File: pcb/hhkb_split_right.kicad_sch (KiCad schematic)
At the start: 82 parts, among them SW1 keyswitch, SW10 keyswitch, SW11 keyswitch, SW12 keyswitch, SW13 keyswitch, SW14 keyswitch, SW15 keyswitch, SW16 keyswitch, SW17 keyswitch, SW18 keyswitch, SW19 keyswitch, SW2 keyswitch, SW20 keyswitch, SW21 keyswitch, SW22 keyswitch, SW23 keyswitch, SW24 keyswitch, SW25 keyswitch, SW26 keyswitch, SW27 keyswitch, SW28 keyswitch, SW29 keyswitch, SW3 keyswitch, SW30 keyswitch, SW31 keyswitch, SW32 keyswitch, SW33 keyswitch, SW34 keyswitch, SW4 keyswitch, SW5 keyswitch, SW6 keyswitch, SW7 keyswitch, SW8 keyswitch, SW9 keyswitch, U1 74LVC595, U2 74LVC595

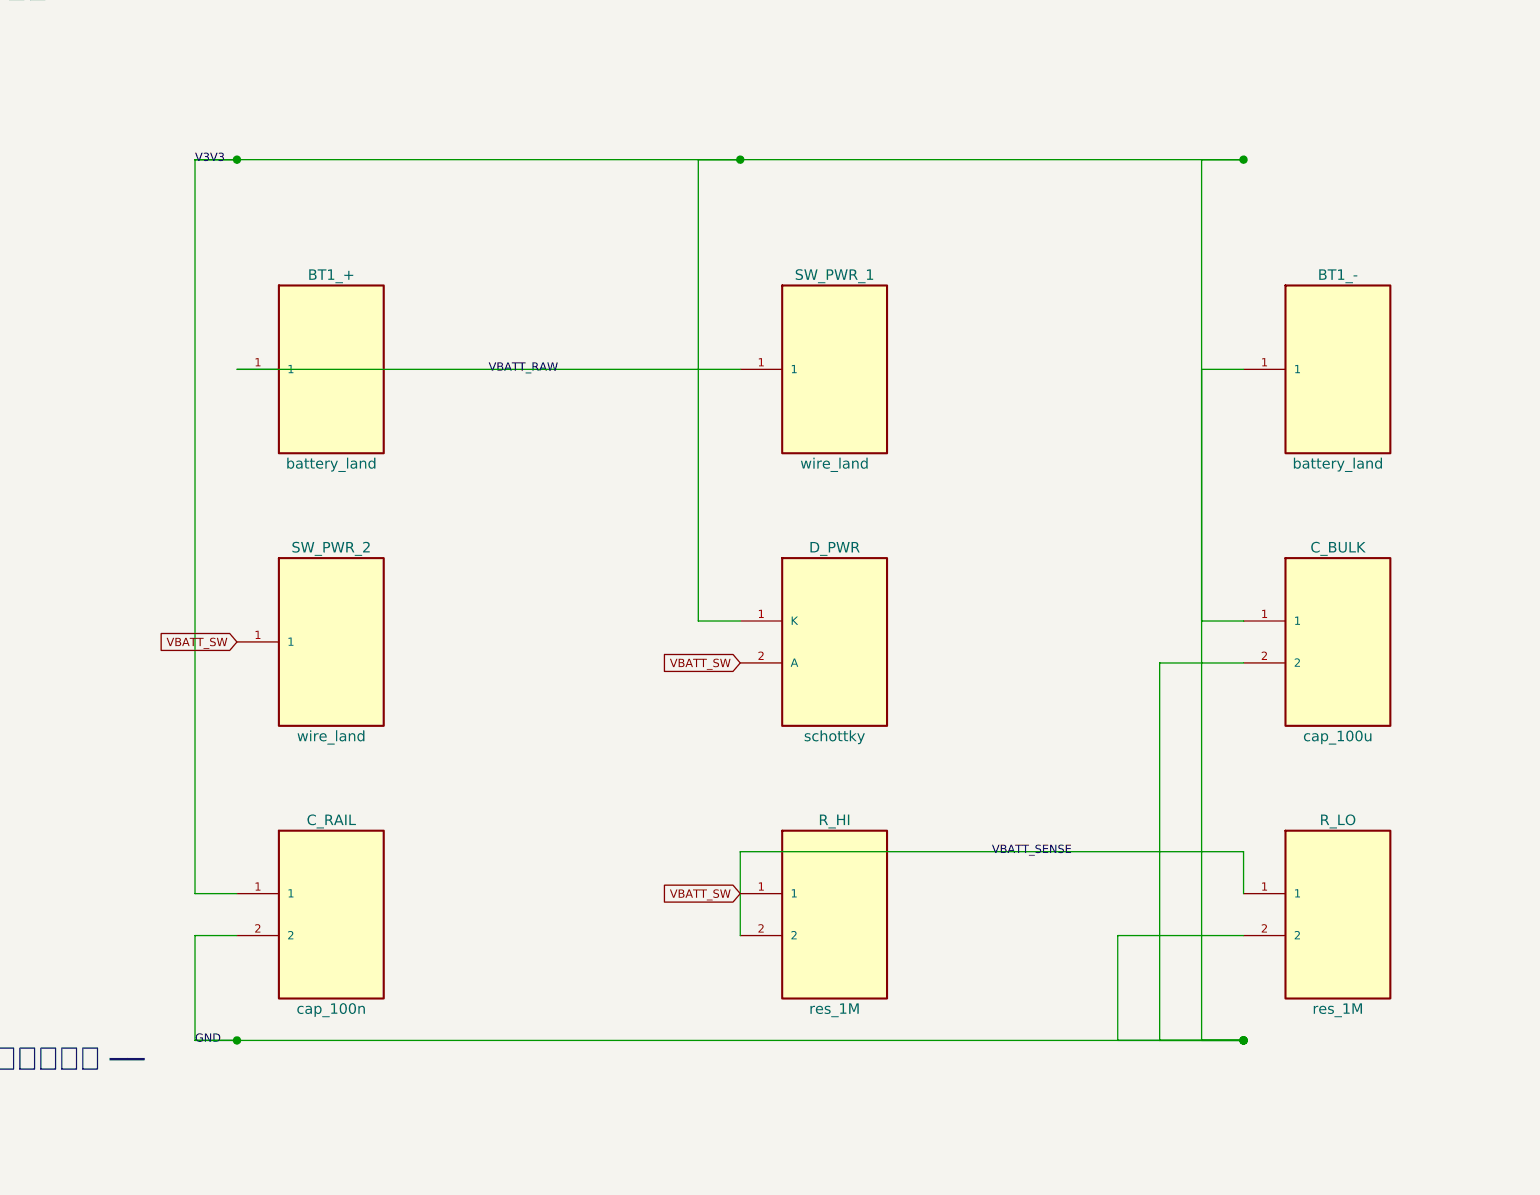
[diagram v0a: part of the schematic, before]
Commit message: C_RAIL を消した。置き場所の根拠が持たず C_U1 の重複だった
open-gaps #39 は「U1 の隣か J_DB の隣か」で止まっていたが、二択の
立て方が違った。FFC の反対側の C_DB を数えると、U_MCU から 3.95mm の
XIAO 用パスコンで、FFC 入口ではない。つまりケーブル入口のパスコンは
もともと両端どちらにも無く、片端だけ手当てする案は理屈が対称にならない。

C_RAIL は実測で J_DB から 70mm、C_U1 の 5.1mm 隣にあった（J_DB を
帯 1 へ移したときに取り残された）。名前どおりの役目は果たしていない。

消した理由は「不要と証明できたから」ではなく、必要と言える根拠が
1 つも無く、各 IC が既に自分の直近パスコンを持つから（595 は
C_U1/C_U2、XIAO は C_DB、レールは C_BULK）。

DRC 違反は左右子とも 0 のまま。右だけ未配線が 0 → 1 に増えた。中身は
信号線ではなく、(152.65, 68.37) の GND スティッチングビアがベタから
浮いたもの（C_RAIL の跡地）。自動配線 2 回で同じなので構造的。
配線に大きな変更が控えているため、それと併せて確認する（open-gaps #40）。

⚠️ pytest tools は最後まで通していない。次の配線変更とまとめて回す。

Co-Authored-By: Claude Opus 5 (1M context) <noreply@anthropic.com>
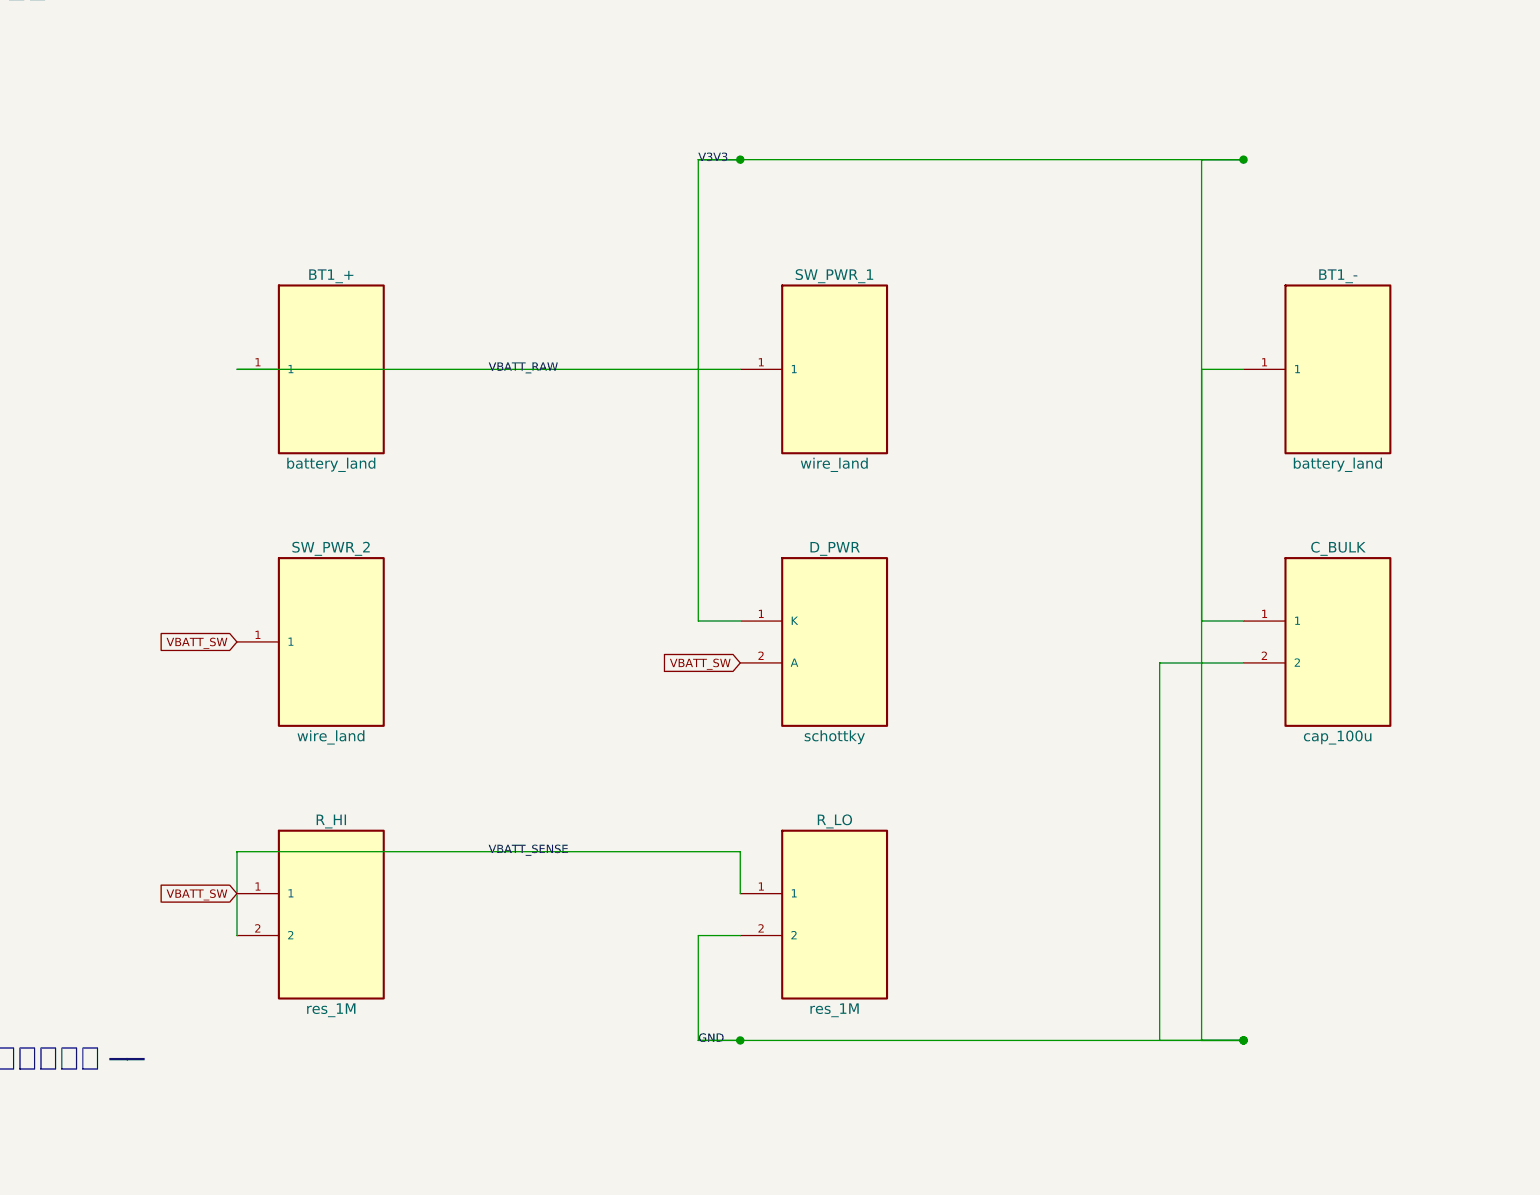
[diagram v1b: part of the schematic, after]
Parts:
- removed C_RAIL: cap_100n, symbol hhkb_split_right:cap_100n
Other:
- moved on the sheet: R_HI, R_LO
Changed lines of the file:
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@@
 		"VBATT_SW"
 		(shape input)
-		(at 124.46 132.08 180)
+		(at 63.50 132.08 180)
 		(effects (font (size 1.0 1.0)))
 	)
@@
 	)
 	(wire
-		(pts (xy 58.42 43.18) (xy 185.42 43.18))
+		(pts (xy 119.38 43.18) (xy 185.42 43.18))
 		(stroke (width 0.508) (type default))
 	)
 	(label
 		"V3V3"
-		(at 58.42 43.18 0)
-		(effects (font (size 1.0 1.0)))
-	)
-	(wire
-		(pts (xy 58.42 149.86) (xy 185.42 149.86))
+		(at 119.38 43.18 0)
+		(effects (font (size 1.0 1.0)))
+	)
+	(wire
+		(pts (xy 119.38 149.86) (xy 185.42 149.86))
 		(stroke (width 0.508) (type default))
 	)
 	(label
 		"GND"
-		(at 58.42 149.86 0)
+		(at 119.38 149.86 0)
 		(effects (font (size 1.0 1.0)))
 	)
@@
 	)
 	(wire
-		(pts (xy 124.46 137.16) (xy 124.46 127.00))
-		(stroke (width 0) (type default))
-	)
-	(wire
-		(pts (xy 124.46 127.00) (xy 185.42 127.00))
-		(stroke (width 0) (type default))
-	)
-	(wire
-		(pts (xy 185.42 127.00) (xy 185.42 132.08))
+		(pts (xy 63.50 137.16) (xy 63.50 127.00))
+		(stroke (width 0) (type default))
+	)
+	(wire
+		(pts (xy 63.50 127.00) (xy 124.46 127.00))
+		(stroke (width 0) (type default))
+	)
+	(wire
+		(pts (xy 124.46 127.00) (xy 124.46 132.08))
 		(stroke (width 0) (type default))
 	)
 	(label
 		"VBATT_SENSE"
-		(at 154.94 127.00 0)
+		(at 93.98 127.00 0)
 		(effects (font (size 1.0 1.0)))
 	)
@@
 	)
 	(wire
-		(pts (xy 63.50 132.08) (xy 58.42 132.08))
-		(stroke (width 0) (type default))
-	)
-	(wire
-		(pts (xy 58.42 132.08) (xy 58.42 43.18))
-		(stroke (width 0) (type default))
-	)
-	(wire
-		(pts (xy 58.42 43.18) (xy 63.50 43.18))
-		(stroke (width 0) (type default))
-	)
-	(junction (at 63.50 43.18) (diameter 1.016) (color 0 0 0 0)
-	)
-	(wire
 		(pts (xy 185.42 68.58) (xy 180.34 68.58))
 		(stroke (width 0) (type default))
@@
 	)
 	(wire
-		(pts (xy 63.50 137.16) (xy 58.42 137.16))
-		(stroke (width 0) (type default))
-	)
-	(wire
-		(pts (xy 58.42 137.16) (xy 58.42 149.86))
-		(stroke (width 0) (type default))
-	)
-	(wire
-		(pts (xy 58.42 149.86) (xy 63.50 149.86))
-		(stroke (width 0) (type default))
-	)
-	(junction (at 63.50 149.86) (diameter 1.016) (color 0 0 0 0)
-	)
-	(wire
-		(pts (xy 185.42 137.16) (xy 170.18 137.16))
-		(stroke (width 0) (type default))
-	)
-	(wire
-		(pts (xy 170.18 137.16) (xy 170.18 149.86))
-		(stroke (width 0) (type default))
-	)
-	(wire
-		(pts (xy 170.18 149.86) (xy 185.42 149.86))
-		(stroke (width 0) (type default))
-	)
-	(junction (at 185.42 149.86) (diameter 1.016) (color 0 0 0 0)
+		(pts (xy 124.46 137.16) (xy 119.38 137.16))
+		(stroke (width 0) (type default))
+	)
+	(wire
+		(pts (xy 119.38 137.16) (xy 119.38 149.86))
+		(stroke (width 0) (type default))
+	)
+	(wire
+		(pts (xy 119.38 149.86) (xy 124.46 149.86))
+		(stroke (width 0) (type default))
+	)
+	(junction (at 124.46 149.86) (diameter 1.016) (color 0 0 0 0)
 	)
 	(wire
@@
 	)
 	(symbol
-		(lib_id "hhkb_split_right:cap_100n")
+		(lib_id "hhkb_split_right:res_1M")
 		(at 74.93 134.62 0)
 		(unit 1)
@@
 		(on_board yes)
 		(dnp no)
-		(property "Reference" "C_RAIL" (at 74.93 123.19 0) (effects (font (size 1.27 1.27))))
-		(property "Value" "cap_100n" (at 74.93 146.05 0) (effects (font (size 1.27 1.27))))
-		(pin "1")
-		(pin "2")
-		(instances
-			(project "hhkb_split_right"
-				(path "/68e5bc58-ebc5-5f0d-bfc6-cc94dff2192d"
-					(reference "C_RAIL")
-					(unit 1)
-				)
-			)
-		)
-	)
-	(symbol
-		(lib_id "hhkb_split_right:res_1M")
-		(at 135.89 134.62 0)
-		(unit 1)
-		(exclude_from_sim no)
-		(in_bom yes)
-		(on_board yes)
-		(dnp no)
-		(property "Reference" "R_HI" (at 135.89 123.19 0) (effects (font (size 1.27 1.27))))
-		(property "Value" "res_1M" (at 135.89 146.05 0) (effects (font (size 1.27 1.27))))
+		(property "Reference" "R_HI" (at 74.93 123.19 0) (effects (font (size 1.27 1.27))))
+		(property "Value" "res_1M" (at 74.93 146.05 0) (effects (font (size 1.27 1.27))))
 		(pin "1")
 		(pin "2")
@@
 	(symbol
 		(lib_id "hhkb_split_right:res_1M")
-		(at 196.85 134.62 0)
+		(at 135.89 134.62 0)
 		(unit 1)
 		(exclude_from_sim no)
@@
 		(on_board yes)
 		(dnp no)
-		(property "Reference" "R_LO" (at 196.85 123.19 0) (effects (font (size 1.27 1.27))))
-		(property "Value" "res_1M" (at 196.85 146.05 0) (effects (font (size 1.27 1.27))))
+		(property "Reference" "R_LO" (at 135.89 123.19 0) (effects (font (size 1.27 1.27))))
+		(property "Value" "res_1M" (at 135.89 146.05 0) (effects (font (size 1.27 1.27))))
 		(pin "1")
 		(pin "2")

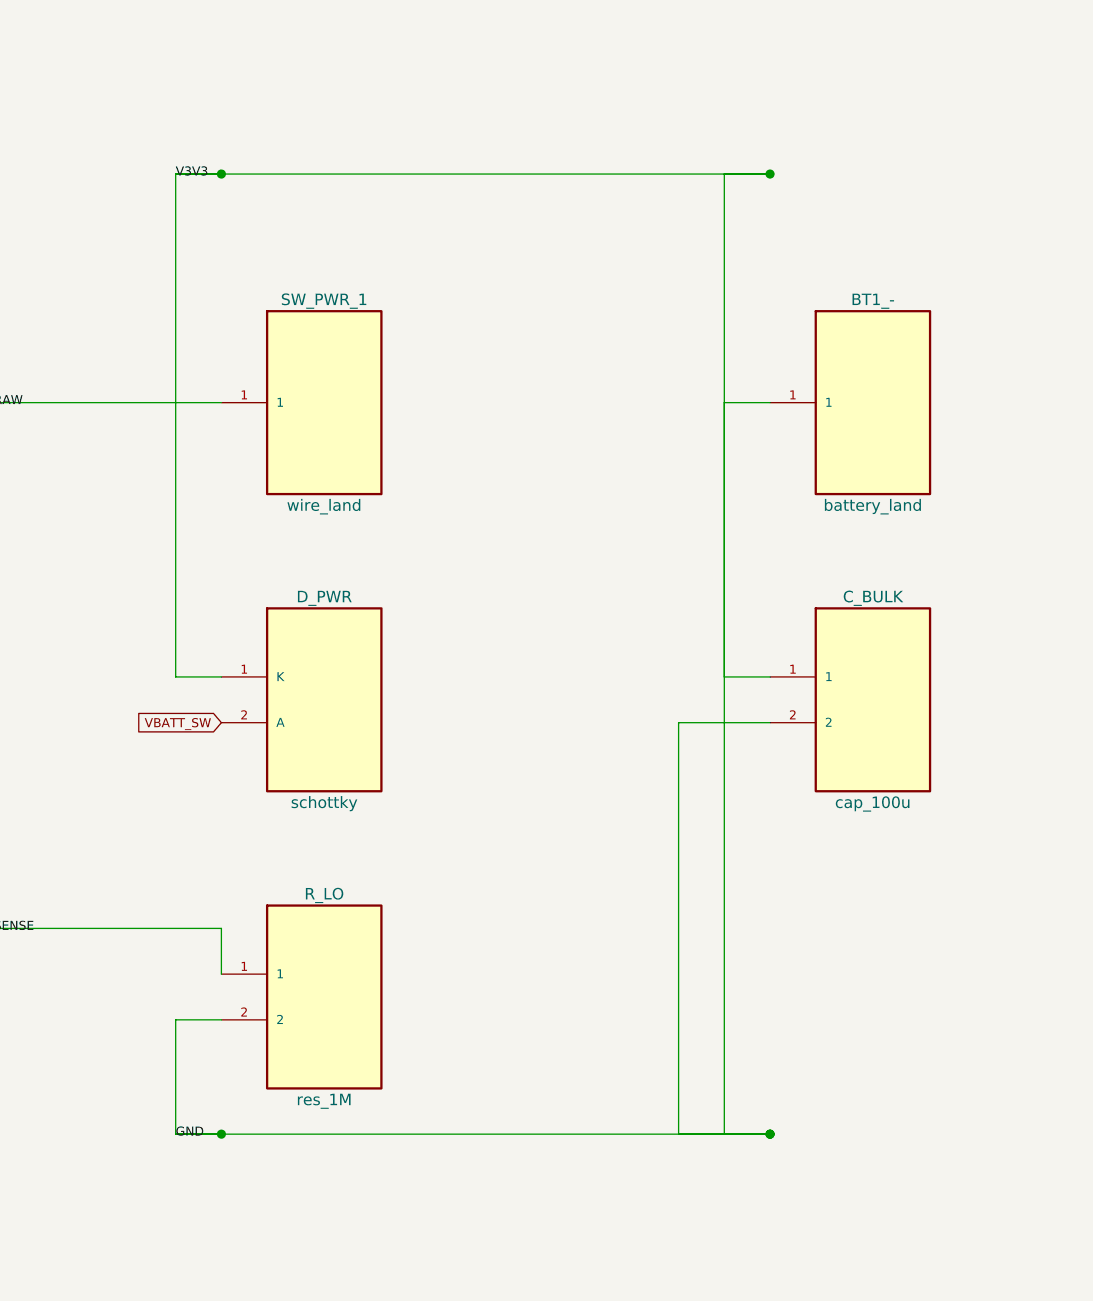
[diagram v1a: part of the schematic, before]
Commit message: バルクを子基板へ移し、電源鎖を消費側へ寄せ、行バスを直線にした
利用者の指摘を順に潰した。どれも「測ったら前提が違っていた」型。

1. バルク（C_BULK）を子基板へ
   守る相手は XIAO の µs 級の電流変動（electrical-design 1-5）で、
   595 でも整流点でもない。XIAO は子基板にいるので、主基板に置くと
   FFC 100mm のインダクタンスの外側から供給することになる。
   XIAO の 3V3 パッドから 2.04mm の位置へ移した。

2. 電源ブロックを V3V3 の消費側へ
   整流点 D_PWR が板の左端にあるのに、消費側（C_U1・U1・J_DB）は
   全部反対側だった。U1 の左へ寄せて V3V3 の銅 132→81mm、
   VBATT_SENSE 110→78mm。左の帯 0 はアンテナ禁止域と取付穴で
   分断されていて、プラス側へは出せない（一度出して DRC 13 件）。

3. 行のバスを裏面の直線で自分で引く（prewire_row_bus）
   ROW0 が 222mm・ビア 7 本・区間 54 で表裏を行き来していた。
   同じ行のダイオードの K 側は y が完全に一致し、ライン上に
   スルーホールが無いので直線が引ける（ROW4 は元から 0 ビアだった）。
   左の未配線 1 本（ROW2）はこれで解決した。
   ⚠️ DSN に (autoroute_settings) を足す道は駄目。左が 66 本に壊れた。

4. アンテナの禁止域（30x15mm）を削除
   利用者の「本当にアンテナの真上ですか」で測ったら、覆っていなかった。
     禁止域 y 30.60..45.60 / 基板後端 48.70 / アンテナ 49.50..53.00
   アンテナは基板の後端より 0.80mm 奥（XIAO_OVERHANG 1.8mm の効果）で、
   平面的に基板の外。禁止域は 3.9mm 的を外したまま 450mm² を捨て、
   左の配線を圧迫していた。
   **根拠に挙げられていた検査は存在しなかった。**interface.py は
   test_the_antenna_keepout_actually_covers_the_antenna が照合すると
   書いていたが、その名前の検査はどこにも無い。実在したのは
   「禁止域の中が空か」だけで、位置は誰も見ていなかった。
   代わりに test_the_antenna_clears_the_main_board を置いた
   （XIAO_OVERHANG を 0 にすると落ちることを確認済み）。

   → open-gaps #23 の幾何の証明（アンテナは必ず 4mm 以上 基板の下に
     入る）は、もう成立していない。ただし余裕は 0.80mm しかないので、
     手 0（アルミ箔で RSSI）の価値は残る。#23 の書き直しは次。

残っているもの（次に着手する）:
  右 未配線 3（GND 離島 1 + V3V3 が J_DB へ届かない 2）★機能的な故障
  左 未配線 1（GND 離島）
  違反はどれも 0。自前配線で塞ぐ案は取らない——今は綺麗に引けても
  配置を変えると黙って壊れ、再現性が無い（利用者の判断）。

pytest tools は未実行。

Co-Authored-By: Claude Opus 5 (1M context) <noreply@anthropic.com>
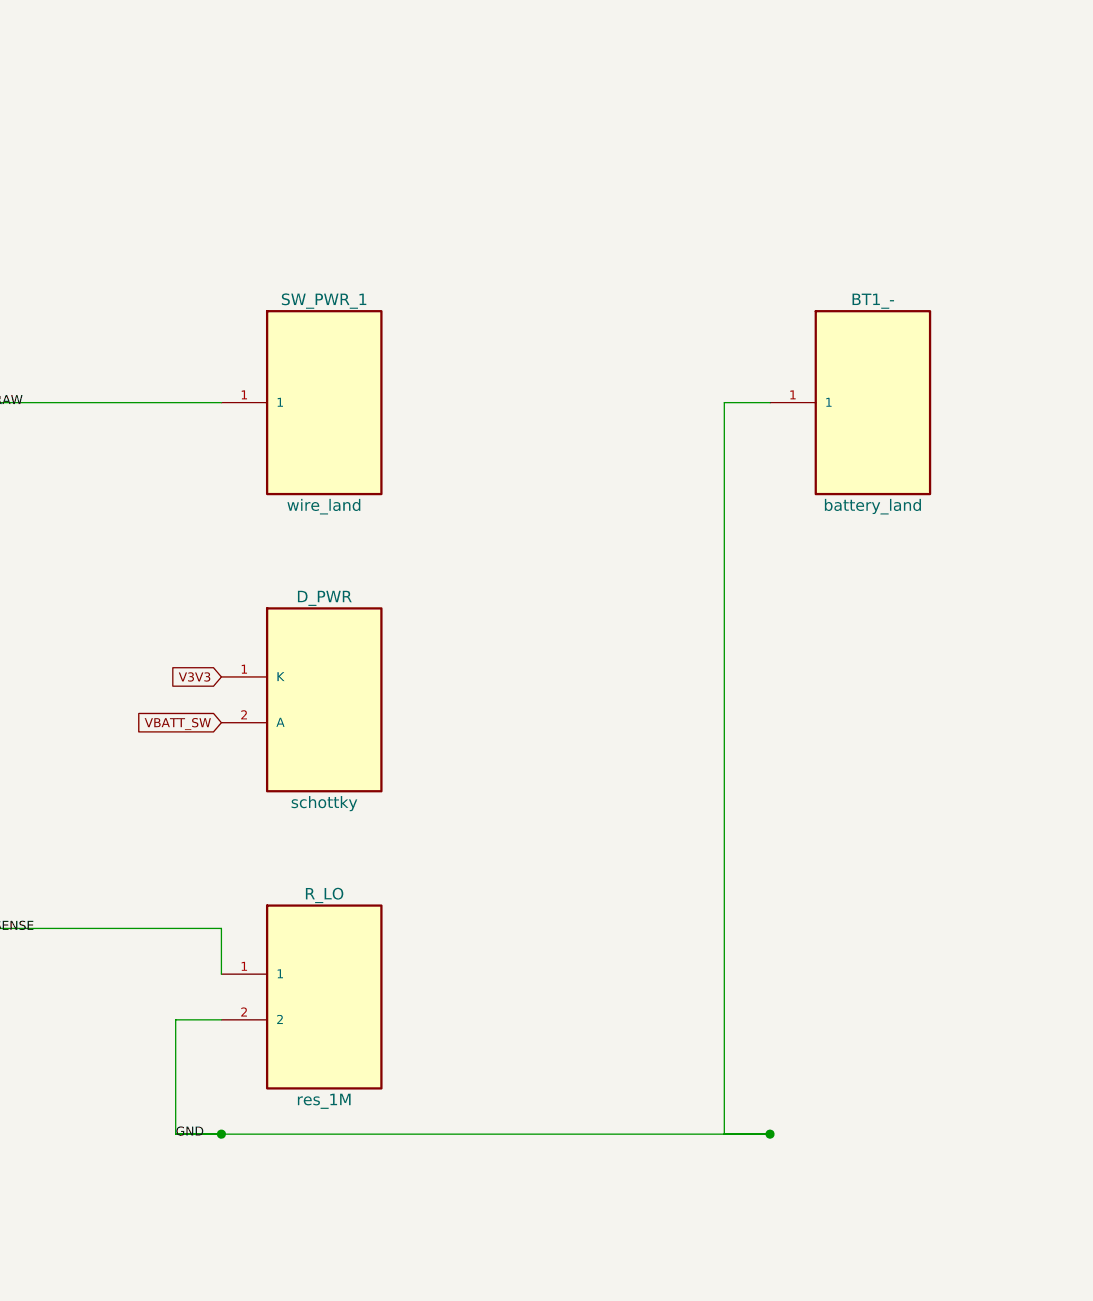
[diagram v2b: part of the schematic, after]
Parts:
- removed C_BULK: cap_100u, symbol hhkb_split_right:cap_100u
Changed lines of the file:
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@@
+	)
+	(global_label
+		"V3V3"
+		(shape input)
+		(at 124.46 99.06 180)
+		(effects (font (size 1.0 1.0)))
 	)
 	(global_label
@@
 	)
 	(wire
-		(pts (xy 119.38 43.18) (xy 185.42 43.18))
-		(stroke (width 0.508) (type default))
-	)
-	(label
-		"V3V3"
-		(at 119.38 43.18 0)
-		(effects (font (size 1.0 1.0)))
-	)
-	(wire
 		(pts (xy 119.38 149.86) (xy 185.42 149.86))
 		(stroke (width 0.508) (type default))
@@
 	)
 	(wire
-		(pts (xy 124.46 99.06) (xy 119.38 99.06))
-		(stroke (width 0) (type default))
-	)
-	(wire
-		(pts (xy 119.38 99.06) (xy 119.38 43.18))
-		(stroke (width 0) (type default))
-	)
-	(wire
-		(pts (xy 119.38 43.18) (xy 124.46 43.18))
-		(stroke (width 0) (type default))
-	)
-	(junction (at 124.46 43.18) (diameter 1.016) (color 0 0 0 0)
-	)
-	(wire
-		(pts (xy 185.42 99.06) (xy 180.34 99.06))
-		(stroke (width 0) (type default))
-	)
-	(wire
-		(pts (xy 180.34 99.06) (xy 180.34 43.18))
-		(stroke (width 0) (type default))
-	)
-	(wire
-		(pts (xy 180.34 43.18) (xy 185.42 43.18))
-		(stroke (width 0) (type default))
-	)
-	(junction (at 185.42 43.18) (diameter 1.016) (color 0 0 0 0)
-	)
-	(wire
 		(pts (xy 185.42 68.58) (xy 180.34 68.58))
 		(stroke (width 0) (type default))
@@
 	(wire
 		(pts (xy 180.34 149.86) (xy 185.42 149.86))
-		(stroke (width 0) (type default))
-	)
-	(junction (at 185.42 149.86) (diameter 1.016) (color 0 0 0 0)
-	)
-	(wire
-		(pts (xy 185.42 104.14) (xy 175.26 104.14))
-		(stroke (width 0) (type default))
-	)
-	(wire
-		(pts (xy 175.26 104.14) (xy 175.26 149.86))
-		(stroke (width 0) (type default))
-	)
-	(wire
-		(pts (xy 175.26 149.86) (xy 185.42 149.86))
 		(stroke (width 0) (type default))
 	)
@@
 					(unit 1)
 				)
-			)
-		)
-	)
-	(symbol
-		(lib_id "hhkb_split_right:cap_100u")
-		(at 196.85 101.60 0)
-		(unit 1)
-		(exclude_from_sim no)
-		(in_bom yes)
-		(on_board yes)
-		(dnp no)
-		(property "Reference" "C_BULK" (at 196.85 90.17 0) (effects (font (size 1.27 1.27))))
-		(property "Value" "cap_100u" (at 196.85 113.03 0) (effects (font (size 1.27 1.27))))
-		(pin "1")
-		(pin "2")
-		(instances
-			(project "hhkb_split_right"
-				(path "/68e5bc58-ebc5-5f0d-bfc6-cc94dff2192d"
-					(reference "C_BULK")
-					(unit 1)
-				)
